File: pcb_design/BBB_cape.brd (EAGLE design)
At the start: 86.4 x 54.6 mm, 4 parts

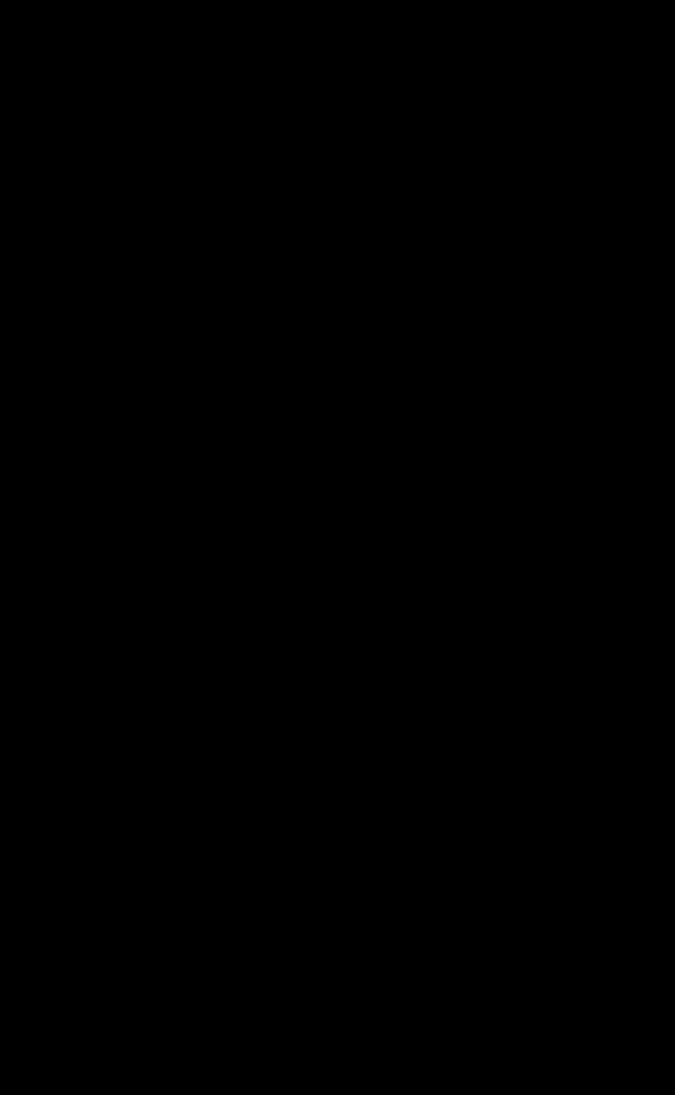
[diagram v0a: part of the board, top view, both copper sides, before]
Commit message: added v6 with better connectors and some small drill changes
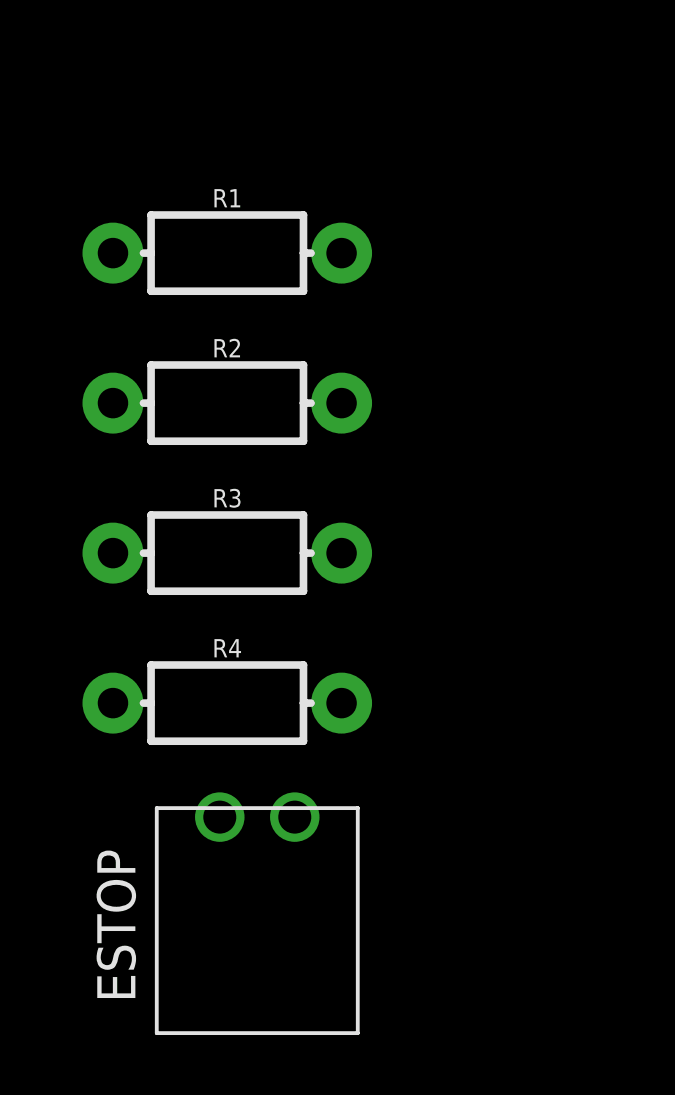
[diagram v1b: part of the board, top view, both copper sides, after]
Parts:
- added ESTOP: PHOENIX_CONNECTOR_1778625, byu_pressure_control:PHOENIX_CONNECTOR_1778625
- added R1, R2, R3, R4: 2.2k, SparkFun-Resistors:AXIAL-0.3-KIT
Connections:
- new net GND: B1.P8.2, B1.P9.1
- net 3V3: now also B1.P9.3, R1.P$2, R2.P$2, R3.P$1, R4.P$2
- net 5V: now also B1.P9.5
- net N$1: no longer B1.P8.17
- net SCL1_L: now also R2.P$1
- net SCL2_L: now also R4.P$1
- net SDA1_L: now also R1.P$1
- net SDA2_L: now also R3.P$2
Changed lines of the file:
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@@
 <attribute name="NAME" x="-29.21" y="60.96" size="1.27" layer="21"/>
+</element>
+<element name="R1" library="SparkFun-Resistors" package="AXIAL-0.3-KIT" value="2.2k" x="-55" y="-5" smashed="yes">
+<attribute name="NAME" x="-55" y="-3.476" size="0.6096" layer="25" font="vector" ratio="20" align="bottom-center"/>
+<attribute name="PROD_ID" value="RES-08380" x="-55" y="-5" size="1.778" layer="27" display="off"/>
+<attribute name="VALUE" x="-55" y="-6.524" size="0.6096" layer="27" font="vector" ratio="20" align="top-center"/>
+</element>
+<element name="R2" library="SparkFun-Resistors" package="AXIAL-0.3-KIT" value="2.2k" x="-55" y="-10" smashed="yes">
+<attribute name="NAME" x="-55" y="-8.476" size="0.6096" layer="25" font="vector" ratio="20" align="bottom-center"/>
+<attribute name="PROD_ID" value="RES-08380" x="-55" y="-10" size="1.778" layer="27" display="off"/>
+<attribute name="VALUE" x="-55" y="-11.524" size="0.6096" layer="27" font="vector" ratio="20" align="top-center"/>
+</element>
+<element name="R3" library="SparkFun-Resistors" package="AXIAL-0.3-KIT" value="2.2k" x="-55" y="-15" smashed="yes">
+<attribute name="NAME" x="-55" y="-13.476" size="0.6096" layer="25" font="vector" ratio="20" align="bottom-center"/>
+<attribute name="PROD_ID" value="RES-08380" x="-55" y="-15" size="1.778" layer="27" display="off"/>
+<attribute name="VALUE" x="-55" y="-16.524" size="0.6096" layer="27" font="vector" ratio="20" align="top-center"/>
+</element>
+<element name="R4" library="SparkFun-Resistors" package="AXIAL-0.3-KIT" value="2.2k" x="-55" y="-20" smashed="yes">
+<attribute name="NAME" x="-55" y="-18.476" size="0.6096" layer="25" font="vector" ratio="20" align="bottom-center"/>
+<attribute name="PROD_ID" value="RES-08380" x="-55" y="-20" size="1.778" layer="27" display="off"/>
+<attribute name="VALUE" x="-55" y="-21.524" size="0.6096" layer="27" font="vector" ratio="20" align="top-center"/>
+</element>
+<element name="ESTOP" library="byu_pressure_control" library_urn="urn:adsk.eagle:library:26800355" package="PHOENIX_CONNECTOR_1778625" package3d_urn="urn:adsk.eagle:package:26802270/3" value="PHOENIX_CONNECTOR_1778625" x="-54" y="-31" smashed="yes">
+<attribute name="AVAILABILITY" value="Good" x="-54" y="-31" size="1.778" layer="27" display="off"/>
+<attribute name="DESCRIPTION" value=" 2 Position Terminal Block Header, Male Pins, Shrouded (4 Side) 0.098 (2.50mm) 90°, Right Angle Through Hole " x="-54" y="-31" size="1.778" layer="27" display="off"/>
+<attribute name="MF" value="Phoenix Contact" x="-54" y="-31" size="1.778" layer="27" display="off"/>
+<attribute name="MP" value="1778625" x="-54" y="-31" size="1.778" layer="27" display="off"/>
+<attribute name="NAME" x="-58.064" y="-29.984" size="1.27" layer="21" rot="R90"/>
+<attribute name="PACKAGE" value="None" x="-54" y="-31" size="1.778" layer="27" display="off"/>
+<attribute name="PRICE" value="None" x="-54" y="-31" size="1.778" layer="27" display="off"/>
+<attribute name="PURCHASE-URL" value="https://pricing.snapeda.com/search/part/1778625/?ref=eda" x="-54" y="-31" size="1.778" layer="27" display="off"/>
 </element>
 </elements>
 <signals>
 <signal name="5V">
+<contactref element="B1" pad="P9.5"/>
 <contactref element="SHIFTER1" pad="10"/>
+<wire x1="25.4" y1="1.905" x2="-21.59" y2="73.66" width="0" layer="19" extent="1-1"/>
 </signal>
 <signal name="3V3">
 <contactref element="SHIFTER1" pad="1"/>
+<contactref element="B1" pad="P9.3"/>
+<contactref element="R1" pad="P$2"/>
+<contactref element="R2" pad="P$2"/>
+<contactref element="R3" pad="P$1"/>
+<contactref element="R4" pad="P$2"/>
+<wire x1="-51.19" y1="-20" x2="-58.81" y2="-15" width="0" layer="19" extent="1-1"/>
+<wire x1="-51.19" y1="-10" x2="-58.81" y2="-15" width="0" layer="19" extent="1-1"/>
+<wire x1="-51.19" y1="-5" x2="-51.19" y2="-10" width="0" layer="19" extent="1-1"/>
+<wire x1="22.86" y1="1.905" x2="-51.19" y2="-5" width="0" layer="19" extent="1-1"/>
+<wire x1="-29.21" y1="73.66" x2="-51.19" y2="-5" width="0" layer="19" extent="1-1"/>
 </signal>
 <signal name="SDA1_L">
 <contactref element="SHIFTER1" pad="2"/>
+<contactref element="R1" pad="P$1"/>
+<wire x1="-29.21" y1="71.12" x2="-58.81" y2="-5" width="0" layer="19" extent="1-1"/>
 </signal>
 <signal name="SCL1_L">
 <contactref element="SHIFTER1" pad="3"/>
+<contactref element="R2" pad="P$1"/>
+<wire x1="-29.21" y1="68.58" x2="-58.81" y2="-10" width="0" layer="19" extent="1-1"/>
 </signal>
 <signal name="SDA2_L">
 <contactref element="SHIFTER1" pad="4"/>
+<contactref element="R3" pad="P$2"/>
+<wire x1="-29.21" y1="66.04" x2="-51.19" y2="-15" width="0" layer="19" extent="1-1"/>
 </signal>
 <signal name="SCL2_L">
 <contactref element="SHIFTER1" pad="5"/>
+<contactref element="R4" pad="P$1"/>
+<wire x1="-29.21" y1="63.5" x2="-58.81" y2="-20" width="0" layer="19" extent="1-1"/>
 </signal>
 <signal name="N$1">
 <contactref element="SHIFTER1" pad="9"/>
 <contactref element="I2C1_OUT" pad="1"/>
-<contactref element="B1" pad="P8.17"/>
-<wire x1="-21.59" y1="71.12" x2="40.64" y2="50.165" width="0" layer="19" extent="1-1"/>
 <wire x1="-45.7" y1="68.16" x2="-21.59" y2="71.12" width="0" layer="19" extent="1-1"/>
 </signal>
@@
 <wire x1="-53.36" y1="68.16" x2="-21.59" y2="63.5" width="0" layer="19" extent="1-1"/>
 </signal>
+<signal name="GND">
+<contactref element="B1" pad="P8.2"/>
+<contactref element="B1" pad="P9.1"/>
+<wire x1="20.32" y1="1.905" x2="20.32" y2="52.705" width="0" layer="19" extent="1-1"/>
+</signal>
 </signals>

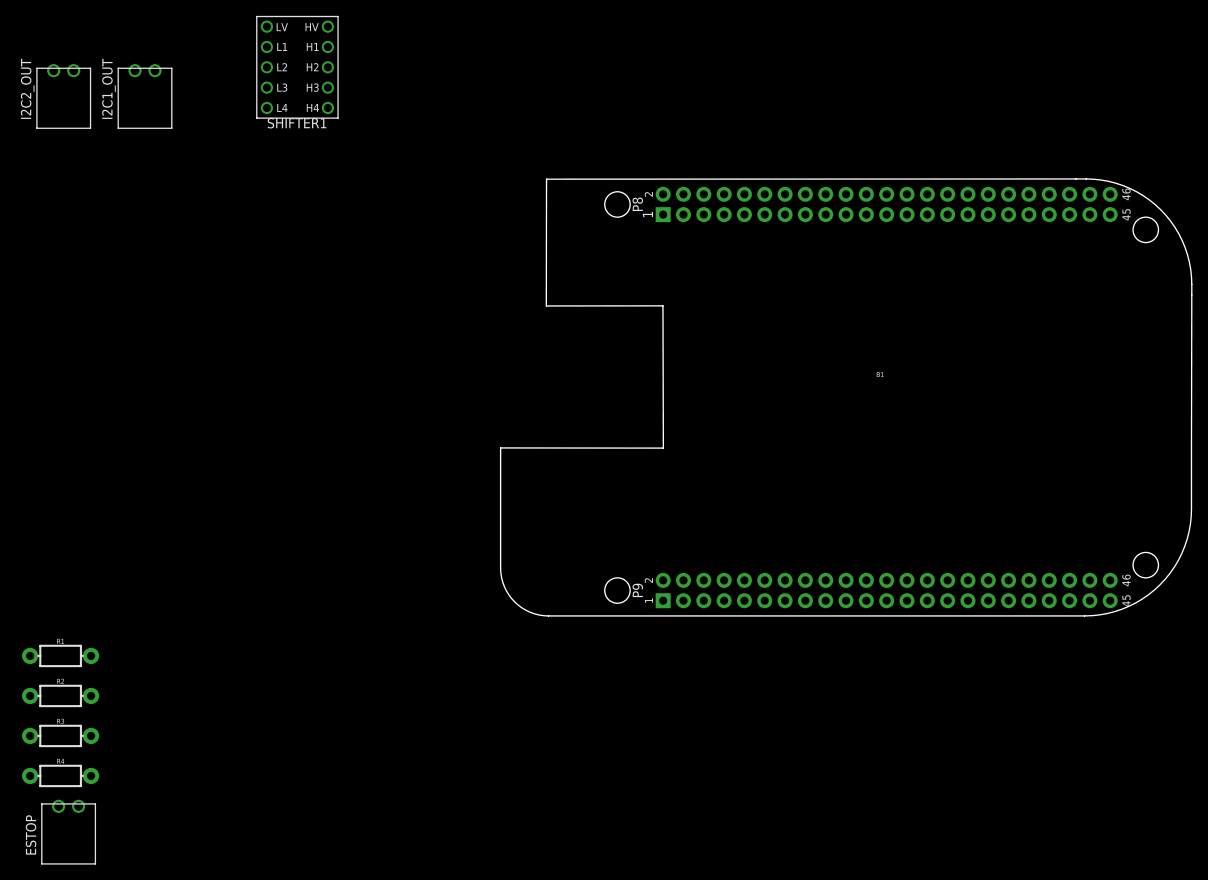
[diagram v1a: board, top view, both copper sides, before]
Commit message: removed old files and updated with CAM files for both pcbs.
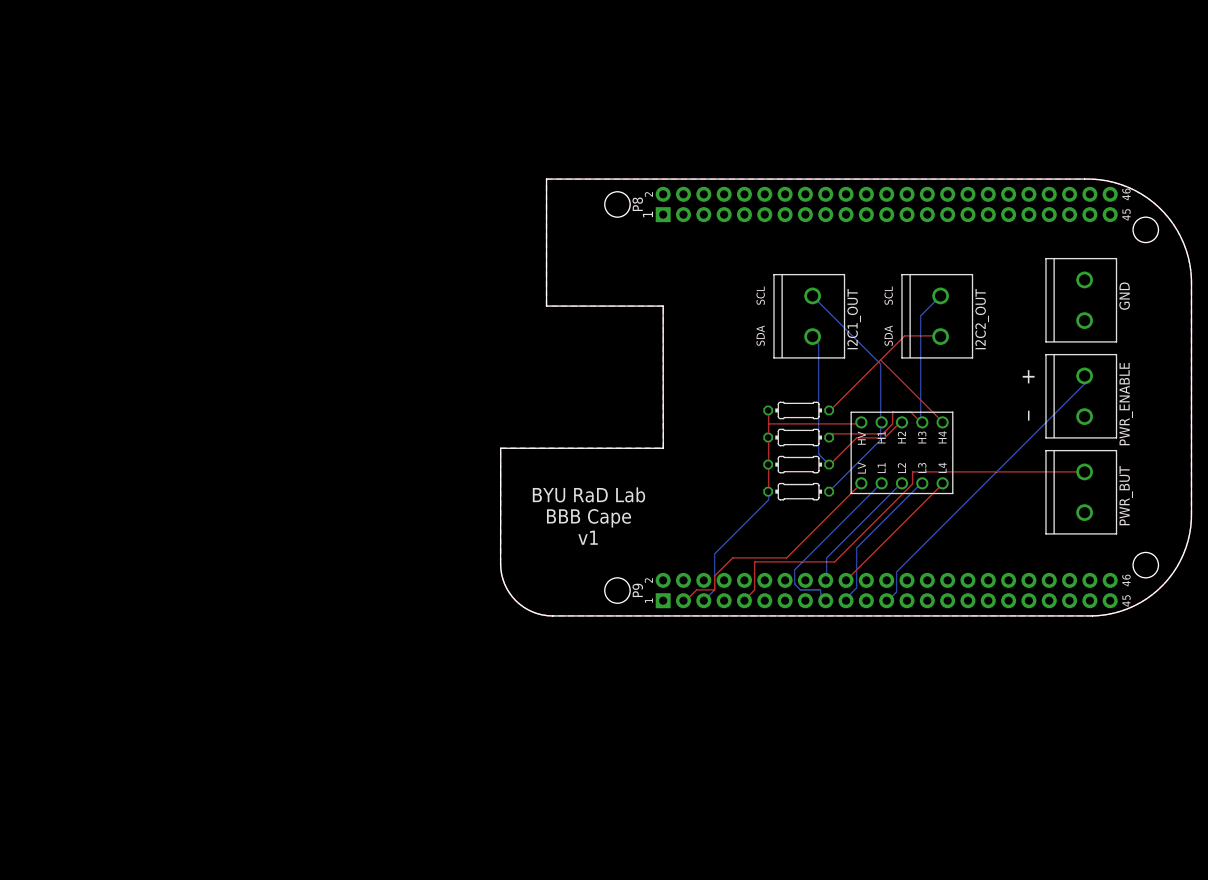
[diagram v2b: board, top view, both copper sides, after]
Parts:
- removed ESTOP: PHOENIX_CONNECTOR_1778625, byu_pressure_control:PHOENIX_CONNECTOR_1778625
- added GND, PWR_BUT, PWR_ENABLE: PHOENIX_CONTACT_1758018, byu_pressure_control:PHOENIX_CONTACT_1758018
- I2C1_OUT, I2C2_OUT: value PHOENIX_CONNECTOR_1778625 -> PHOENIX_CONTACT_1758018; device byu_pressure_control:PHOENIX_CONNECTOR_1778625 -> byu_pressure_control:PHOENIX_CONTACT_1758018
- R1, R2, R3, R4: value 2.2k -> 1.8k; device SparkFun-Resistors:AXIAL-0.3-KIT -> rcl:0204/7
- moved I2C2_OUT 111.6 mm to (55.0, 40.0), turned to 90 degrees
- moved R4 102.9 mm to (37.3, 25.7), turned to 180 degrees
- moved R3 99.5 mm to (37.3, 22.3), turned to 180 degrees
- moved SHIFTER1 98.8 mm to (56.5, 15.3), turned to 90 degrees
- moved R2 96.7 mm to (37.3, 18.9), turned to 180 degrees
- moved R1 94.5 mm to (37.3, 15.5), turned to 180 degrees
- moved I2C1_OUT 86.0 mm to (39.0, 40.0), turned to 90 degrees
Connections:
- removed net 3V3: B1.P9.3, R1.P$2, R2.P$2, R3.P$1, R4.P$2, SHIFTER1.1
- removed net SCL1_L: R2.P$1, SHIFTER1.3
- removed net SCL2_L: R4.P$1, SHIFTER1.5
- removed net SDA1_L: R1.P$1, SHIFTER1.2
- removed net SDA2_L: R3.P$2, SHIFTER1.4
- new net 3.3V: B1.P9.3, SHIFTER1.1
- new net I2C1_SCL: B1.P9.17, SHIFTER1.2
- new net I2C1_SDA: B1.P9.18, SHIFTER1.3
- new net I2C2_SCL: B1.P9.19, SHIFTER1.4
- new net I2C2_SDA: B1.P9.20, SHIFTER1.5
- new net N$5: B1.P9.23, PWR_ENABLE.2
- new net N$6: B1.P9.9, PWR_BUT.2
- net 5V: now also R1.2, R2.2, R3.2, R4.2
- net GND: now also B1.P8.1, B1.P9.2, GND.1, GND.2, PWR_BUT.1, PWR_ENABLE.1
- net N$1: now also I2C1_OUT.2, R1.1; no longer I2C1_OUT.1
- net N$2: now also I2C1_OUT.1, R2.1; no longer I2C1_OUT.2
- net N$3: now also I2C2_OUT.2, R3.1; no longer I2C2_OUT.1
- net N$4: now also I2C2_OUT.1, R4.1; no longer I2C2_OUT.2
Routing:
- net N$6: track 0.00 -> 52.2 mm
- net 5V: track 0.00 -> 39.0 mm
- net N$5: track 0.00 -> 38.4 mm
- net N$3: track 0.00 -> 31.4 mm
- net N$1: track 0.00 -> 30.8 mm
- net 3.3V: track 0.00 -> 29.3 mm
- net N$4: track 0.00 -> 28.9 mm
- net N$2: track 0.00 -> 28.1 mm
- net I2C1_SCL: track 0.00 -> 22.3 mm
- net I2C2_SCL: track 0.00 -> 18.7 mm
- net I2C2_SDA: track 0.00 -> 17.1 mm
- net I2C1_SDA: track 0.00 -> 16.1 mm
- added copper zone on layer 1, net GND
- added copper zone on layer 16, net GND
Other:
- outline, holes or cut-outs redrawn
- board text added: "+"
- board text added: "BYU RaD Lab BBB Cape v1"
- board text added: "SCL"
- board text added: "SDA"
- board text added: "_"

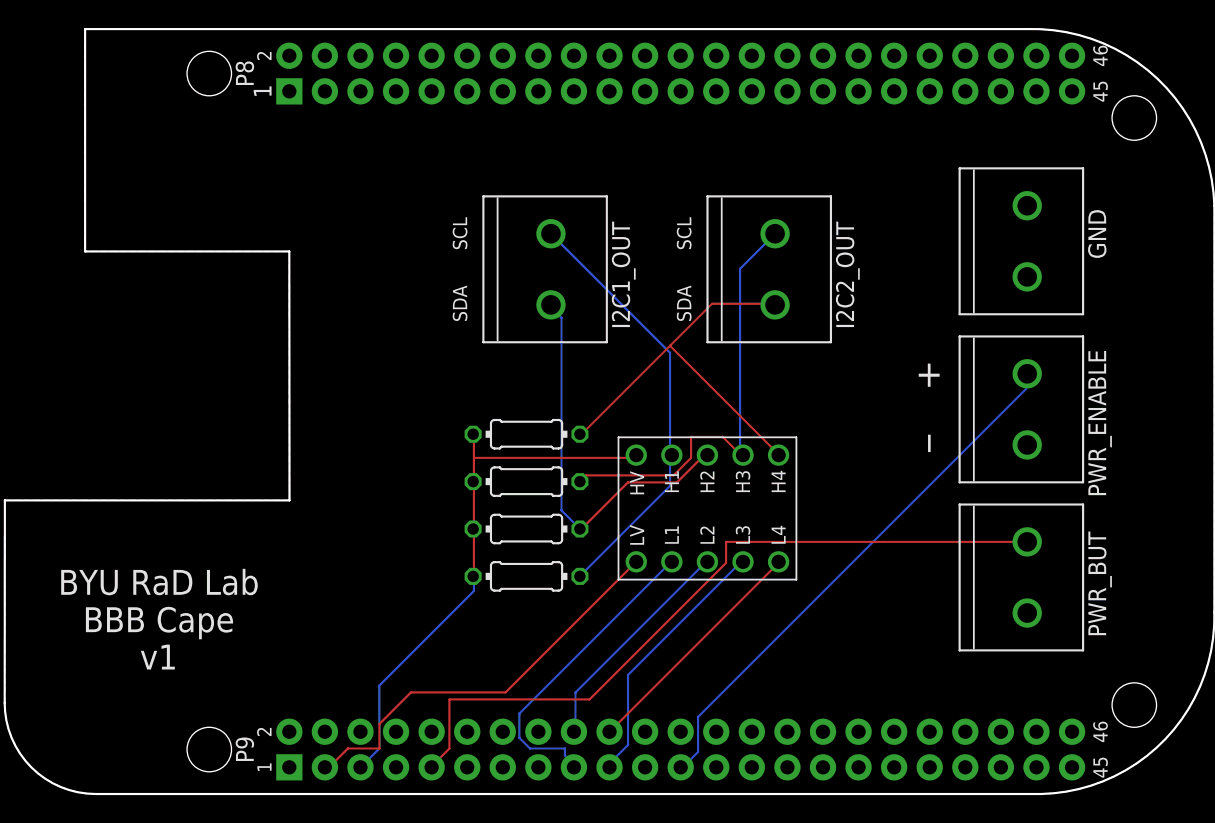
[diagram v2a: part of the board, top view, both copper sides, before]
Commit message: fixed spacing in bbb cape
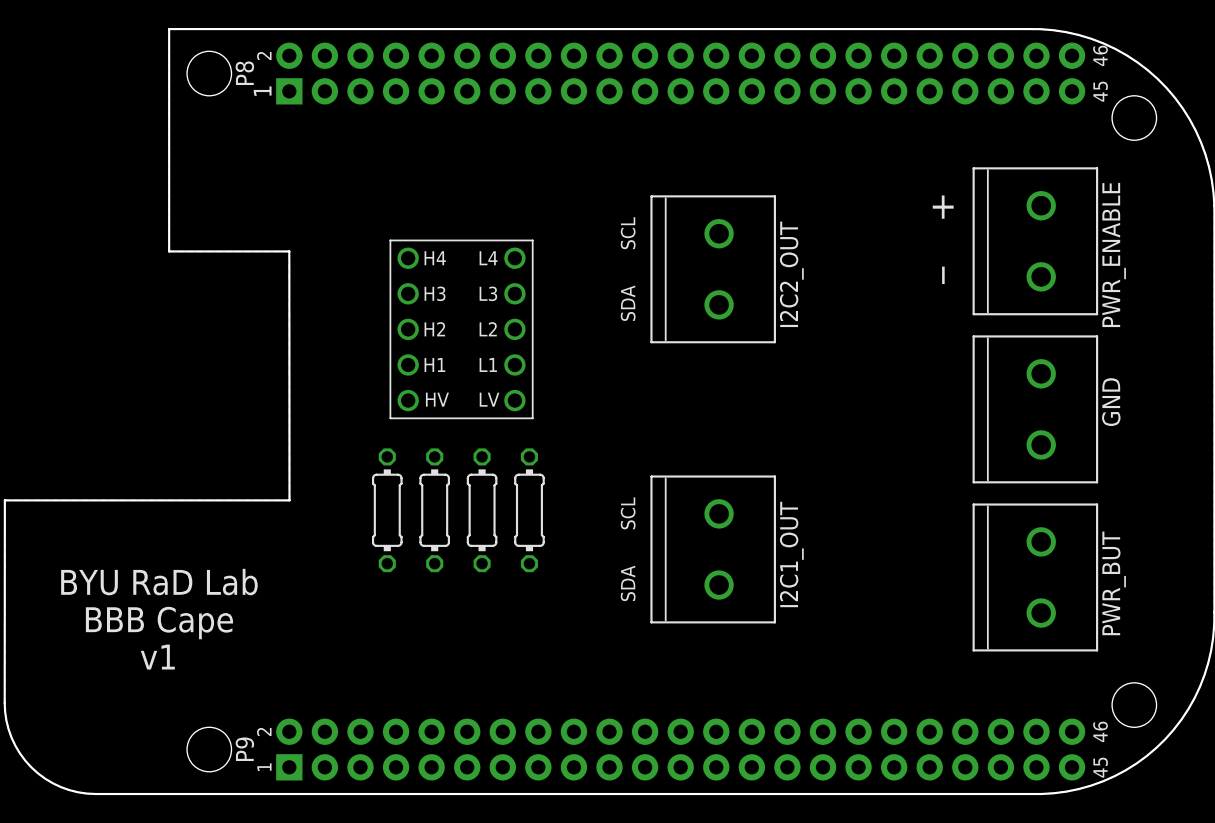
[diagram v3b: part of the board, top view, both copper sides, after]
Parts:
- moved SHIFTER1 30.7 mm to (37.7, 39.5), turned to 180 degrees
- moved I2C1_OUT 23.3 mm to (51.0, 20.0)
- moved GND 12.0 mm to (74.0, 30.0)
- moved PWR_ENABLE 12.0 mm to (74.0, 42.0)
- moved R4 11.3 mm to (27.3, 20.3), turned to 270 degrees
- moved R3 6.87 mm to (30.7, 20.3), turned to 270 degrees
- moved R1 4.72 mm to (37.5, 20.3), turned to 270 degrees
- moved I2C2_OUT 4.00 mm to (51.0, 40.0)
- moved R2 3.44 mm to (34.1, 20.3), turned to 270 degrees
- moved PWR_BUT 1.00 mm to (74.0, 18.0)
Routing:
- net N$6: track 52.2 -> 0.00 mm
- net 5V: track 39.0 -> 0.00 mm
- net N$5: track 38.4 -> 0.00 mm
- net N$3: track 31.4 -> 0.00 mm
- net N$1: track 30.8 -> 0.00 mm
- net 3.3V: track 29.3 -> 0.00 mm
- net N$4: track 28.9 -> 0.00 mm
- net N$2: track 28.1 -> 0.00 mm
- net I2C1_SCL: track 22.3 -> 0.00 mm
- net I2C2_SCL: track 18.7 -> 0.00 mm
- net I2C2_SDA: track 17.1 -> 0.00 mm
- net I2C1_SDA: track 16.1 -> 0.00 mm
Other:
- outline, holes or cut-outs redrawn
- board text added: "<-- from relay"
- board text added: "to estop -->"

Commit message: updated files and cams
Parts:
- R1, R2, R3, R4: value 1.8k -> 2.2k
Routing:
- net N$6: track 0.00 -> 56.1 mm
- net N$5: track 0.00 -> 50.8 mm
- net N$4: track 0.00 -> 40.6 mm
- net N$3: track 0.00 -> 39.7 mm
- net I2C2_SDA: track 0.00 -> 38.7 mm
- net I2C2_SCL: track 0.00 -> 37.7 mm
- net 3.3V: track 0.00 -> 37.7 mm
- net 5V: track 0.00 -> 37.4 mm
- net I2C1_SCL: track 0.00 -> 34.0 mm
- net I2C1_SDA: track 0.00 -> 32.2 mm
- net N$2: track 0.00 -> 32.0 mm
- net N$1: track 0.00 -> 26.6 mm
